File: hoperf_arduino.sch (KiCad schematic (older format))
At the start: 15 parts, among them J1 Conn_01x08_Male, J2 Conn_01x08_Male, SW1 SW_SPST, U1 AZ1117-3.3, U2 RFM95W-915S2

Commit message: update sch and added routed pcb
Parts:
- removed J1, J2: Conn_01x08_Male, Connector_PinHeader_2.54mm:PinHeader_1x08_P2.54mm_Vertical, symbol Connector:Conn_01x08_Male
- added BT1: Battery_Cell, Connector_PinSocket_2.54mm:PinSocket_1x02_P2.54mm_Vertical, symbol Device:Battery_Cell
- U2: footprint RF_Module:HOPERF_RFM9XW_SMD -> RF_Module:HOPERF_RFM9XW_THT
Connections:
- net +5V: now also BT1.1 (+)
- net GND: now also BT1.2 (-)
- net H_DIO2: now also A1.7 (D4)
- net H_DIO3: now also A1.8 (D5)
- net H_DIO4: now also A1.9 (D6)
- net H_DIO5: now also A1.10 (D7)
- net H_RESET: now also A1.12 (D9); no longer A1.8 (D5)
- no-connect marks 0 -> 14
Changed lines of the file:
@@
 F 0 "U2" H 1400 6131 50  0000 C CNN
 F 1 "RFM95W-915S2" H 1400 6040 50  0000 C CNN
-F 2 "RF_Module:HOPERF_RFM9XW_SMD" H -1900 7100 50  0001 C CNN
+F 2 "RF_Module:HOPERF_RFM9XW_THT" H -1900 7100 50  0001 C CNN
 F 3 "https://www.hoperf.com/data/upload/portal/20181127/5bfcbea20e9ef.pdf" H -1900 7100 50  0001 C CNN
 	1    1400 5450
@@
 Wire Wire Line
 	900  5150 600  5150
-$Comp
-L Connector:Conn_01x08_Male J1
-U 1 1 60974A0D
-P 800 1350
-F 0 "J1" H 850 1800 50  0000 C CNN
-F 1 "Conn_01x08_Male" V 700 1300 50  0000 C CNN
-F 2 "Connector_PinHeader_2.54mm:PinHeader_1x08_P2.54mm_Vertical" H 800 1350 50  0001 C CNN
-F 3 "~" H 800 1350 50  0001 C CNN
-	1    800  1350
-	1    0    0    -1
-$EndComp
-Wire Wire Line
-	1000 1250 1300 1250
 Text Label 2700 1100 0    50   ~ 0
 H_MOSI
 Text Label 4150 1100 2    50   ~ 0
 L_MOSI
-Wire Wire Line
-	1000 1350 1300 1350
-Wire Wire Line
-	1000 1450 1300 1450
-Wire Wire Line
-	1000 1550 1300 1550
-Wire Wire Line
-	1000 1650 1300 1650
-Text Label 1300 1250 2    50   ~ 0
-H_MOSI
-Text Label 1300 1350 2    50   ~ 0
-H_MISO
-Text Label 1300 1450 2    50   ~ 0
-H_SCK
-Text Label 1300 1550 2    50   ~ 0
-H_CS
-Text Label 1300 1650 2    50   ~ 0
-H_RESET
-Wire Wire Line
-	1000 1750 1300 1750
-$Comp
-L power:GND #PWR04
-U 1 1 60BAF865
-P 1300 1850
-F 0 "#PWR04" H 1300 1600 50  0001 C CNN
-F 1 "GND" H 1305 1677 50  0000 C CNN
-F 2 "" H 1300 1850 50  0001 C CNN
-F 3 "" H 1300 1850 50  0001 C CNN
-	1    1300 1850
-	1    0    0    -1
-$EndComp
-Wire Wire Line
-	1300 1850 1300 1750
-Wire Wire Line
-	1000 1150 1300 1150
-$Comp
-L power:+5V #PWR03
-U 1 1 60BD2F48
-P 1300 1000
-F 0 "#PWR03" H 1300 850 50  0001 C CNN
-F 1 "+5V" H 1315 1173 50  0000 C CNN
-F 2 "" H 1300 1000 50  0001 C CNN
-F 3 "" H 1300 1000 50  0001 C CNN
-	1    1300 1000
-	1    0    0    -1
-$EndComp
-Wire Wire Line
-	1300 1000 1300 1150
 Wire Notes Line
 	6500 500  6500 3500
@@
 Text Notes 2500 650  0    50   ~ 10
 Bidirectional Level Translator (5V <-> 3V3)
-$Comp
-L Connector:Conn_01x08_Male J2
-U 1 1 60CD0A4F
-P 2150 1350
-F 0 "J2" H 2200 1800 50  0000 C CNN
-F 1 "Conn_01x08_Male" V 2050 1300 50  0000 C CNN
-F 2 "Connector_PinHeader_2.54mm:PinHeader_1x08_P2.54mm_Vertical" H 2150 1350 50  0001 C CNN
-F 3 "~" H 2150 1350 50  0001 C CNN
-	1    2150 1350
-	-1   0    0    -1
-$EndComp
-Wire Wire Line
-	1950 1750 1600 1750
-Wire Wire Line
-	1600 1750 1600 1850
-$Comp
-L power:GND #PWR07
-U 1 1 60CEB7E3
-P 1600 1850
-F 0 "#PWR07" H 1600 1600 50  0001 C CNN
-F 1 "GND" H 1605 1677 50  0000 C CNN
-F 2 "" H 1600 1850 50  0001 C CNN
-F 3 "" H 1600 1850 50  0001 C CNN
-	1    1600 1850
-	1    0    0    -1
-$EndComp
-Wire Wire Line
-	1950 1650 1600 1650
-Wire Wire Line
-	1600 1550 1950 1550
-Wire Wire Line
-	1950 1450 1600 1450
-Wire Wire Line
-	1600 1350 1950 1350
-Wire Wire Line
-	1950 1250 1600 1250
-Wire Wire Line
-	1600 1150 1950 1150
-Wire Wire Line
-	1950 1050 1600 1050
-Wire Wire Line
-	1600 1050 1600 1000
-$Comp
-L power:+3V3 #PWR06
-U 1 1 60D41F77
-P 1600 1000
-F 0 "#PWR06" H 1600 850 50  0001 C CNN
-F 1 "+3V3" H 1615 1173 50  0000 C CNN
-F 2 "" H 1600 1000 50  0001 C CNN
-F 3 "" H 1600 1000 50  0001 C CNN
-	1    1600 1000
-	1    0    0    -1
-$EndComp
-Text Label 1600 1150 0    50   ~ 0
-L_DIO0
-Text Label 1600 1250 0    50   ~ 0
-L_DIO1
-Text Label 1600 1350 0    50   ~ 0
-L_DIO2
-Text Label 1600 1450 0    50   ~ 0
-L_DIO3
-Text Label 1600 1550 0    50   ~ 0
-L_DIO4
-Text Label 1600 1650 0    50   ~ 0
-L_DIO5
-$Comp
-L power:+3V3 #PWR02
-U 1 1 60BD22A2
-P 1050 1000
-F 0 "#PWR02" H 1050 850 50  0001 C CNN
-F 1 "+3V3" H 1065 1173 50  0000 C CNN
-F 2 "" H 1050 1000 50  0001 C CNN
-F 3 "" H 1050 1000 50  0001 C CNN
-	1    1050 1000
-	1    0    0    -1
-$EndComp
-Wire Wire Line
-	1050 1050 1050 1000
-Wire Wire Line
-	1000 1050 1050 1050
 Wire Notes Line
 	2400 2100 500  2100
@@
 Text Label 6000 1500 2    50   ~ 0
 L_DIO1
-$Comp
-L MCU_Module:Arduino_Nano_v3.x A1
-U 1 1 60C9E5C4
-P 10150 3900
-F 0 "A1" H 10150 2811 50  0000 C CNN
-F 1 "Arduino_Nano_v3.x" H 10150 2720 50  0000 C CNN
-F 2 "Module:Arduino_Nano" H 10150 3900 50  0001 C CIN
-F 3 "http://www.mouser.com/pdfdocs/Gravitech_Arduino_Nano3_0.pdf" H 10150 3900 50  0001 C CNN
-	1    10150 3900
-	1    0    0    -1
-$EndComp
 Text Label 9250 4400 0    50   ~ 0
 H_MOSI
@@
 Text Label 9250 4600 0    50   ~ 0
 H_SCK
-Text Label 9250 3800 0    50   ~ 0
+Text Label 9250 4200 0    50   ~ 0
 H_RESET
 Wire Wire Line
@@
 	9250 3600 9650 3600
 Wire Wire Line
-	9250 3800 9650 3800
+	9250 4200 9650 4200
 Wire Wire Line
 	9250 4300 9650 4300
@@
 Wire Wire Line
 	8300 2850 8300 2750
+NoConn ~ 9650 3400
+NoConn ~ 9650 3300
+NoConn ~ 10250 2900
+NoConn ~ 10350 2900
+NoConn ~ 10650 3400
+NoConn ~ 10650 3700
+NoConn ~ 10650 4000
+NoConn ~ 10650 4100
+NoConn ~ 10650 4200
+NoConn ~ 10650 4300
+NoConn ~ 10650 4400
+NoConn ~ 10650 4500
+$Comp
+L MCU_Module:Arduino_Nano_v3.x A1
+U 1 1 60C9E5C4
+P 10150 3900
+F 0 "A1" H 10150 2811 50  0000 C CNN
+F 1 "Arduino_Nano_v3.x" H 10150 2720 50  0000 C CNN
+F 2 "Module:Arduino_Nano" H 10150 3900 50  0001 C CIN
+F 3 "http://www.mouser.com/pdfdocs/Gravitech_Arduino_Nano3_0.pdf" H 10150 3900 50  0001 C CNN
+	1    10150 3900
+	1    0    0    -1
+$EndComp
+Text Label 9250 3700 0    50   ~ 0
+H_DIO2
+Text Label 9250 3800 0    50   ~ 0
+H_DIO3
+Text Label 9250 3900 0    50   ~ 0
+H_DIO4
+Text Label 9250 4000 0    50   ~ 0
+H_DIO5
+Wire Wire Line
+	9650 3700 9250 3700
+Wire Wire Line
+	9250 3800 9650 3800
+Wire Wire Line
+	9650 3900 9250 3900
+Wire Wire Line
+	9650 4000 9250 4000
+NoConn ~ 9650 4100
+NoConn ~ 10650 4600
+$Comp
+L Device:Battery_Cell BT1
+U 1 1 60DF8C4E
+P 7950 4250
+F 0 "BT1" V 8205 4300 50  0000 C CNN
+F 1 "Battery_Cell" V 8114 4300 50  0000 C CNN
+F 2 "Connector_PinSocket_2.54mm:PinSocket_1x02_P2.54mm_Vertical" V 7950 4310 50  0001 C CNN
+F 3 "~" V 7950 4310 50  0001 C CNN
+	1    7950 4250
+	0    -1   -1   0
+$EndComp
+$Comp
+L power:+5V #PWR0129
+U 1 1 60DF950D
+P 7600 4250
+F 0 "#PWR0129" H 7600 4100 50  0001 C CNN
+F 1 "+5V" V 7615 4378 50  0000 L CNN
+F 2 "" H 7600 4250 50  0001 C CNN
+F 3 "" H 7600 4250 50  0001 C CNN
+	1    7600 4250
+	0    -1   -1   0
+$EndComp
+$Comp
+L power:GND #PWR0130
+U 1 1 60DF9FE7
+P 8200 4250
+F 0 "#PWR0130" H 8200 4000 50  0001 C CNN
+F 1 "GND" V 8205 4122 50  0000 R CNN
+F 2 "" H 8200 4250 50  0001 C CNN
+F 3 "" H 8200 4250 50  0001 C CNN
+	1    8200 4250
+	0    -1   -1   0
+$EndComp
+Wire Wire Line
+	8200 4250 8050 4250
+Wire Wire Line
+	7750 4250 7600 4250
 $EndSCHEMATC

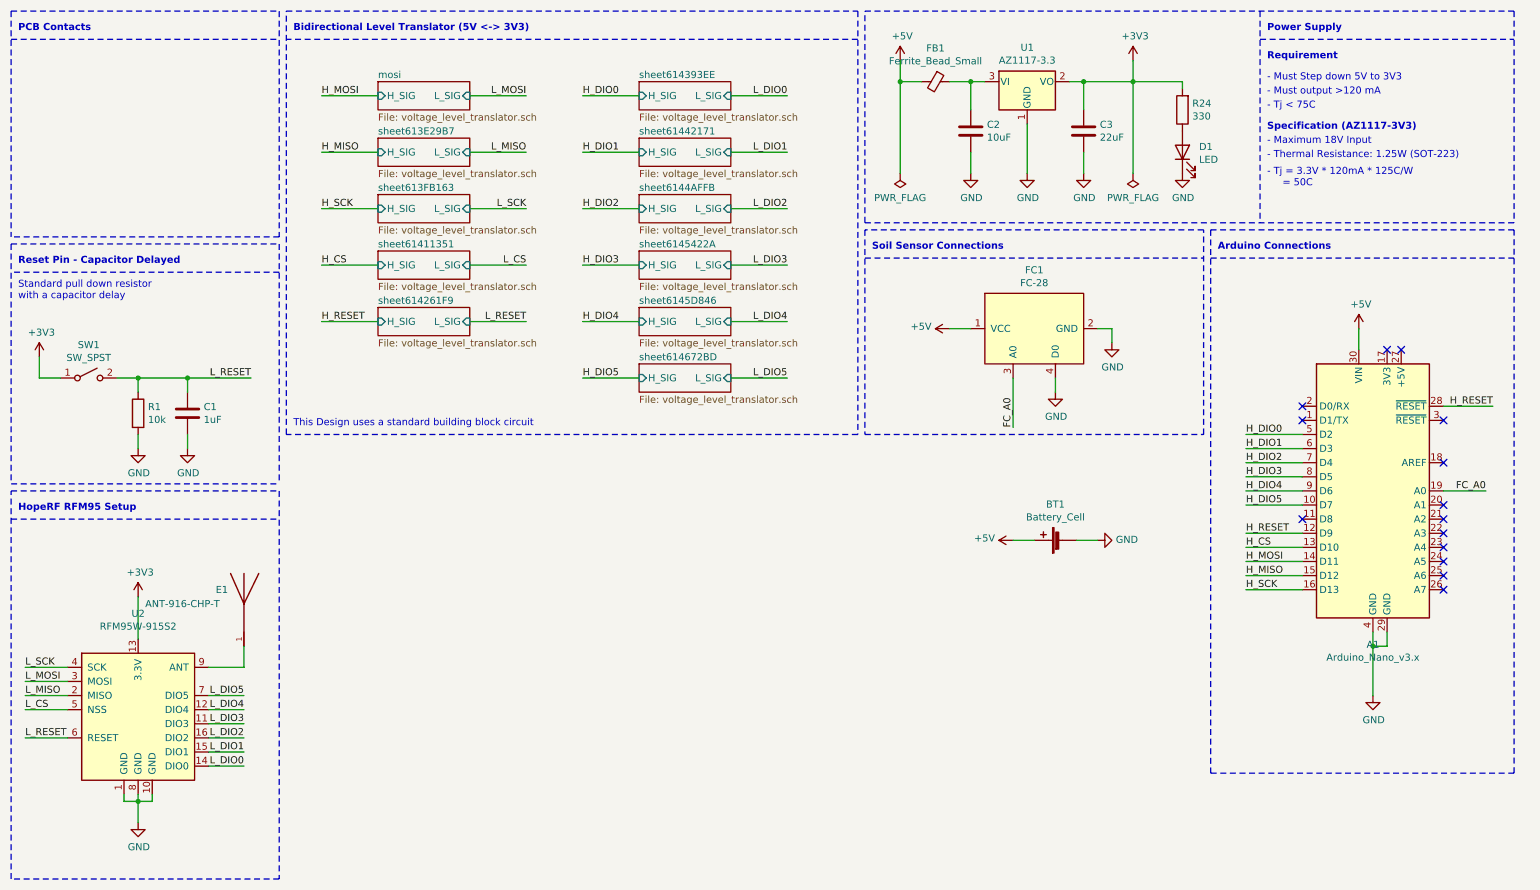
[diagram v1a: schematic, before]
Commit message: remove unncessary parts, update sch
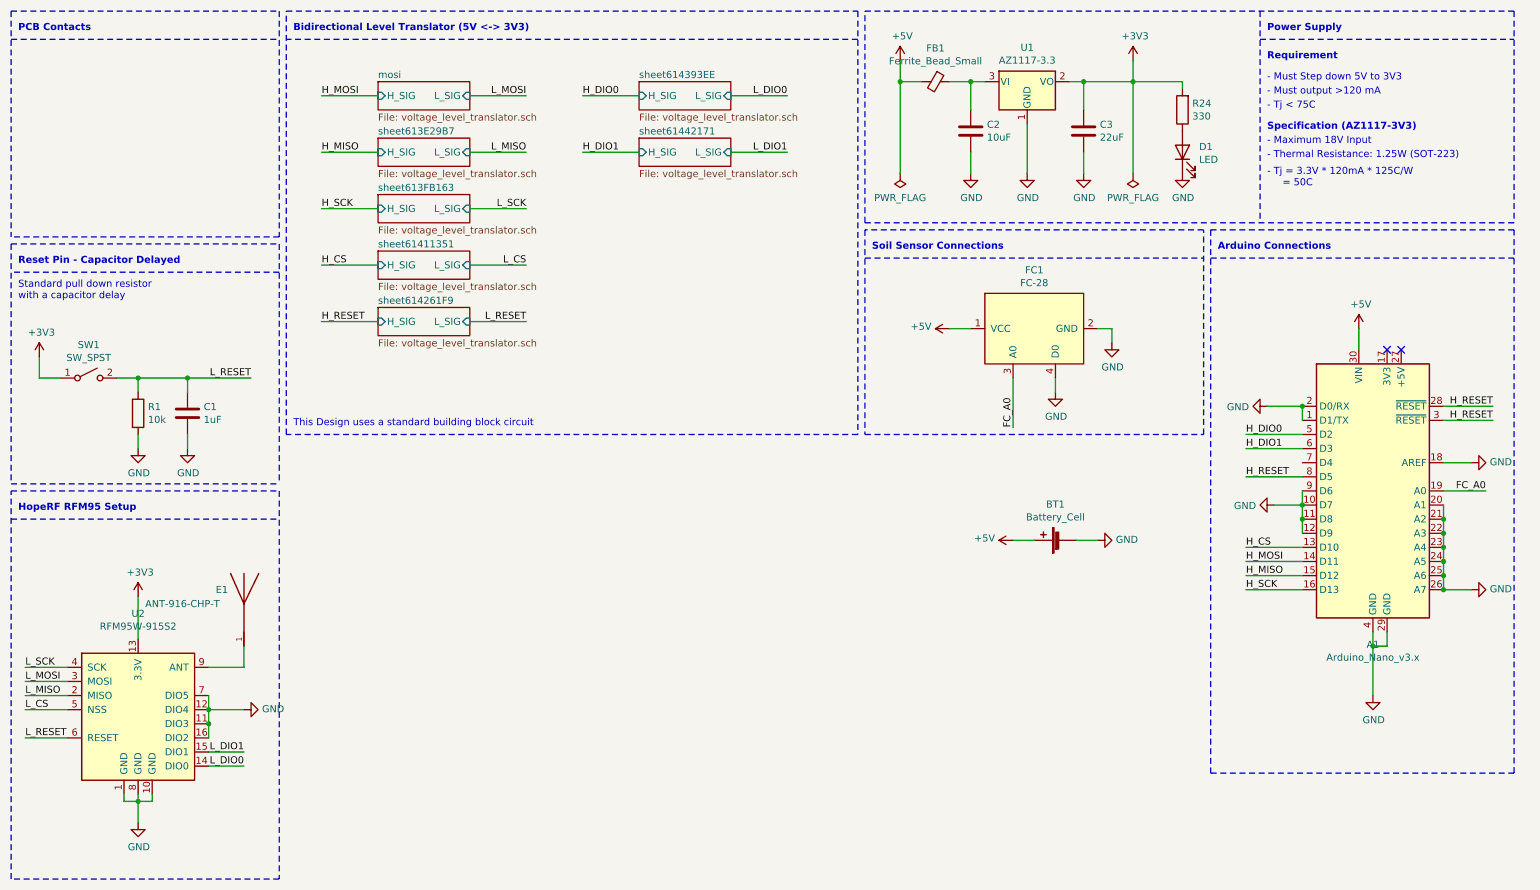
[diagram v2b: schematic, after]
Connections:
- net H_DIO3 is gone; now on net H_RESET: A1.8 (D5)
- net H_DIO4 is gone; now on net GND: A1.9 (D6)
- net H_DIO5 is gone; now on net GND: A1.10 (D7)
- net L_DIO2 is gone; now on net GND: U2.16 (DIO2)
- net L_DIO3 is gone; now on net GND: U2.11 (DIO3)
- net L_DIO4 is gone; now on net GND: U2.12 (DIO4)
- net L_DIO5 is gone; now on net GND: U2.7 (DIO5)
- net GND: now also A1.1 (D1/TX), A1.11 (D8), A1.12 (D9), A1.18 (AREF), A1.2 (D0/RX), A1.20 (A1), A1.21 (A2), A1.22 (A3), A1.23 (A4), A1.24 (A5), A1.25 (A6), A1.26 (A7)
- net H_RESET: now also A1.3 (~RESET); no longer A1.12 (D9)
- net H_DIO2: no longer names the net of A1.7 (D4)
- no-connect marks 14 -> 2
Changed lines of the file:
@@
 $Descr A4 11693 8268
 encoding utf-8
-Sheet 1 12
+Sheet 1 8
 Title ""
 Date ""
@@
 Wire Wire Line
 	900  5650 600  5650
-Wire Wire Line
-	1900 5350 2150 5350
-Wire Wire Line
-	1900 5450 2150 5450
-Wire Wire Line
-	1900 5550 2150 5550
-Wire Wire Line
-	1900 5650 2150 5650
 Wire Wire Line
 	1900 5750 2150 5750
@@
 Wire Notes Line
 	500  500  2400 500
-Text Label 2150 5650 2    50   ~ 0
-L_DIO2
-Text Label 2150 5550 2    50   ~ 0
-L_DIO3
-Text Label 2150 5450 2    50   ~ 0
-L_DIO4
-Text Label 2150 5350 2    50   ~ 0
-L_DIO5
 Text Label 2150 5750 2    50   ~ 0
 L_DIO1
@@
 Wire Wire Line
 	4950 1500 4550 1500
-$Sheet
-S 4950 1800 650  200
-U 6144AFFF
-F0 "sheet6144AFFB" 50
-F1 "voltage_level_translator.sch" 50
-F2 "L_SIG" I R 5600 1900 50
-F3 "H_SIG" I L 4950 1900 50
-$EndSheet
-Wire Wire Line
-	5600 1900 6000 1900
-Wire Wire Line
-	4950 1900 4550 1900
-$Sheet
-S 4950 2200 650  200
-U 6145422E
-F0 "sheet6145422A" 50
-F1 "voltage_level_translator.sch" 50
-F2 "L_SIG" I R 5600 2300 50
-F3 "H_SIG" I L 4950 2300 50
-$EndSheet
-Wire Wire Line
-	5600 2300 6000 2300
-Wire Wire Line
-	4950 2300 4550 2300
-$Sheet
-S 4950 2600 650  200
-U 6145D84A
-F0 "sheet6145D846" 50
-F1 "voltage_level_translator.sch" 50
-F2 "L_SIG" I R 5600 2700 50
-F3 "H_SIG" I L 4950 2700 50
-$EndSheet
-Wire Wire Line
-	5600 2700 6000 2700
-Wire Wire Line
-	4950 2700 4550 2700
-$Sheet
-S 4950 3000 650  200
-U 614672C1
-F0 "sheet614672BD" 50
-F1 "voltage_level_translator.sch" 50
-F2 "L_SIG" I R 5600 3100 50
-F3 "H_SIG" I L 4950 3100 50
-$EndSheet
-Wire Wire Line
-	5600 3100 6000 3100
-Wire Wire Line
-	4950 3100 4550 3100
 Text Label 4550 1500 0    50   ~ 0
 H_DIO1
-Text Label 4550 1900 0    50   ~ 0
-H_DIO2
-Text Label 4550 2300 0    50   ~ 0
-H_DIO3
-Text Label 4550 2700 0    50   ~ 0
-H_DIO4
-Text Label 4550 3100 0    50   ~ 0
-H_DIO5
-Text Label 6000 3100 2    50   ~ 0
-L_DIO5
-Text Label 6000 2700 2    50   ~ 0
-L_DIO4
-Text Label 6000 2300 2    50   ~ 0
-L_DIO3
-Text Label 6000 1900 2    50   ~ 0
-L_DIO2
 Text Label 6000 1500 2    50   ~ 0
 L_DIO1
@@
 Text Label 9250 4600 0    50   ~ 0
 H_SCK
-Text Label 9250 4200 0    50   ~ 0
+Text Label 9250 3800 0    50   ~ 0
 H_RESET
 Wire Wire Line
@@
 	9250 3600 9650 3600
 Wire Wire Line
-	9250 4200 9650 4200
+	9250 3800 9650 3800
 Wire Wire Line
 	9250 4300 9650 4300
@@
 Wire Wire Line
 	8300 2850 8300 2750
-NoConn ~ 9650 3400
-NoConn ~ 9650 3300
 NoConn ~ 10250 2900
 NoConn ~ 10350 2900
-NoConn ~ 10650 3400
-NoConn ~ 10650 3700
-NoConn ~ 10650 4000
-NoConn ~ 10650 4100
-NoConn ~ 10650 4200
-NoConn ~ 10650 4300
-NoConn ~ 10650 4400
-NoConn ~ 10650 4500
 $Comp
 L MCU_Module:Arduino_Nano_v3.x A1
@@
 	1    0    0    -1
 $EndComp
-Text Label 9250 3700 0    50   ~ 0
-H_DIO2
-Text Label 9250 3800 0    50   ~ 0
-H_DIO3
-Text Label 9250 3900 0    50   ~ 0
-H_DIO4
-Text Label 9250 4000 0    50   ~ 0
-H_DIO5
-Wire Wire Line
-	9650 3700 9250 3700
-Wire Wire Line
-	9250 3800 9650 3800
-Wire Wire Line
-	9650 3900 9250 3900
-Wire Wire Line
-	9650 4000 9250 4000
-NoConn ~ 9650 4100
-NoConn ~ 10650 4600
 $Comp
 L Device:Battery_Cell BT1
@@
 Wire Wire Line
 	7750 4250 7600 4250
+Text Label 11000 3400 2    50   ~ 0
+H_RESET
+Wire Wire Line
+	11000 3400 10650 3400
+$Comp
+L power:GND #PWR?
+U 1 1 60E78F09
+P 9450 4000
+F 0 "#PWR?" H 9450 3750 50  0001 C CNN
+F 1 "GND" V 9455 3872 50  0000 R CNN
+F 2 "" H 9450 4000 50  0001 C CNN
+F 3 "" H 9450 4000 50  0001 C CNN
+	1    9450 4000
+	0    1    1    0
+$EndComp
+Wire Wire Line
+	9650 3900 9650 4000
+Connection ~ 9650 4000
+Wire Wire Line
+	9650 4000 9650 4100
+Connection ~ 9650 4100
+Wire Wire Line
+	9650 4100 9650 4200
+Wire Wire Line
+	9650 4000 9450 4000
+$Comp
+L power:GND #PWR?
+U 1 1 60E80D17
+P 9400 3300
+F 0 "#PWR?" H 9400 3050 50  0001 C CNN
+F 1 "GND" V 9405 3172 50  0000 R CNN
+F 2 "" H 9400 3300 50  0001 C CNN
+F 3 "" H 9400 3300 50  0001 C CNN
+	1    9400 3300
+	0    1    1    0
+$EndComp
+Wire Wire Line
+	9650 3300 9650 3400
+Wire Wire Line
+	9650 3300 9400 3300
+Connection ~ 9650 3300
+$Comp
+L power:GND #PWR?
+U 1 1 60E89E88
+P 2150 5450
+F 0 "#PWR?" H 2150 5200 50  0001 C CNN
+F 1 "GND" V 2155 5322 50  0000 R CNN
+F 2 "" H 2150 5450 50  0001 C CNN
+F 3 "" H 2150 5450 50  0001 C CNN
+	1    2150 5450
+	0    -1   -1   0
+$EndComp
+Wire Wire Line
+	1900 5350 1900 5450
+Connection ~ 1900 5450
+Wire Wire Line
+	1900 5450 1900 5550
+Connection ~ 1900 5550
+Wire Wire Line
+	1900 5550 1900 5650
+Wire Wire Line
+	1900 5450 2150 5450
+$Comp
+L power:GND #PWR?
+U 1 1 60E8EC5C
+P 10850 3700
+F 0 "#PWR?" H 10850 3450 50  0001 C CNN
+F 1 "GND" V 10855 3572 50  0000 R CNN
+F 2 "" H 10850 3700 50  0001 C CNN
+F 3 "" H 10850 3700 50  0001 C CNN
+	1    10850 3700
+	0    -1   -1   0
+$EndComp
+Wire Wire Line
+	10650 3700 10850 3700
+$Comp
+L power:GND #PWR?
+U 1 1 60E917A2
+P 10850 4600
+F 0 "#PWR?" H 10850 4350 50  0001 C CNN
+F 1 "GND" V 10855 4472 50  0000 R CNN
+F 2 "" H 10850 4600 50  0001 C CNN
+F 3 "" H 10850 4600 50  0001 C CNN
+	1    10850 4600
+	0    -1   -1   0
+$EndComp
+Wire Wire Line
+	10650 4600 10650 4500
+Connection ~ 10650 4100
+Wire Wire Line
+	10650 4100 10650 4000
+Connection ~ 10650 4200
+Wire Wire Line
+	10650 4200 10650 4100
+Connection ~ 10650 4300
+Wire Wire Line
+	10650 4300 10650 4200
+Connection ~ 10650 4400
+Wire Wire Line
+	10650 4400 10650 4300
+Connection ~ 10650 4500
+Wire Wire Line
+	10650 4500 10650 4400
+Wire Wire Line
+	10650 4600 10850 4600
+Connection ~ 10650 4600
 $EndSCHEMATC
